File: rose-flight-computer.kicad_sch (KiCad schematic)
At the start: 17 parts

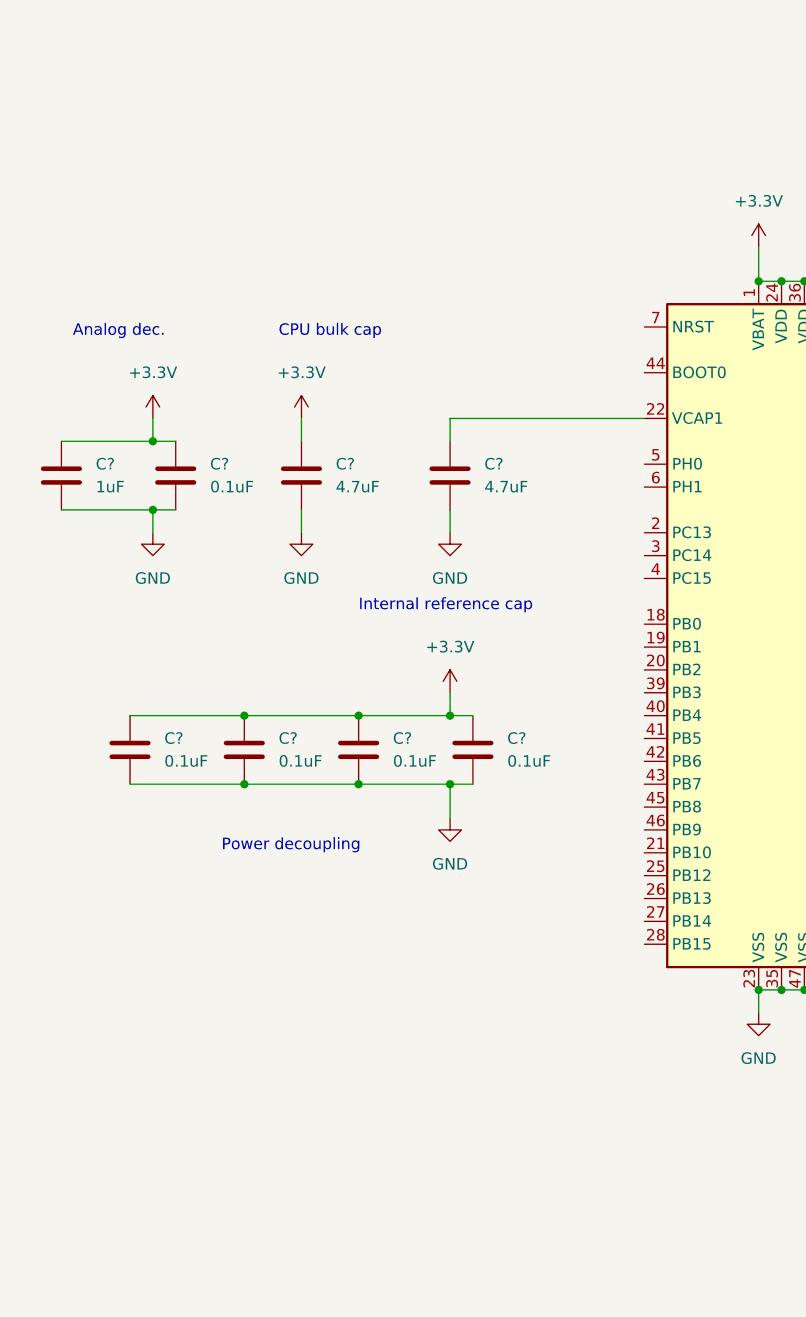
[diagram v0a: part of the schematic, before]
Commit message: Imported power circuit from old schematic
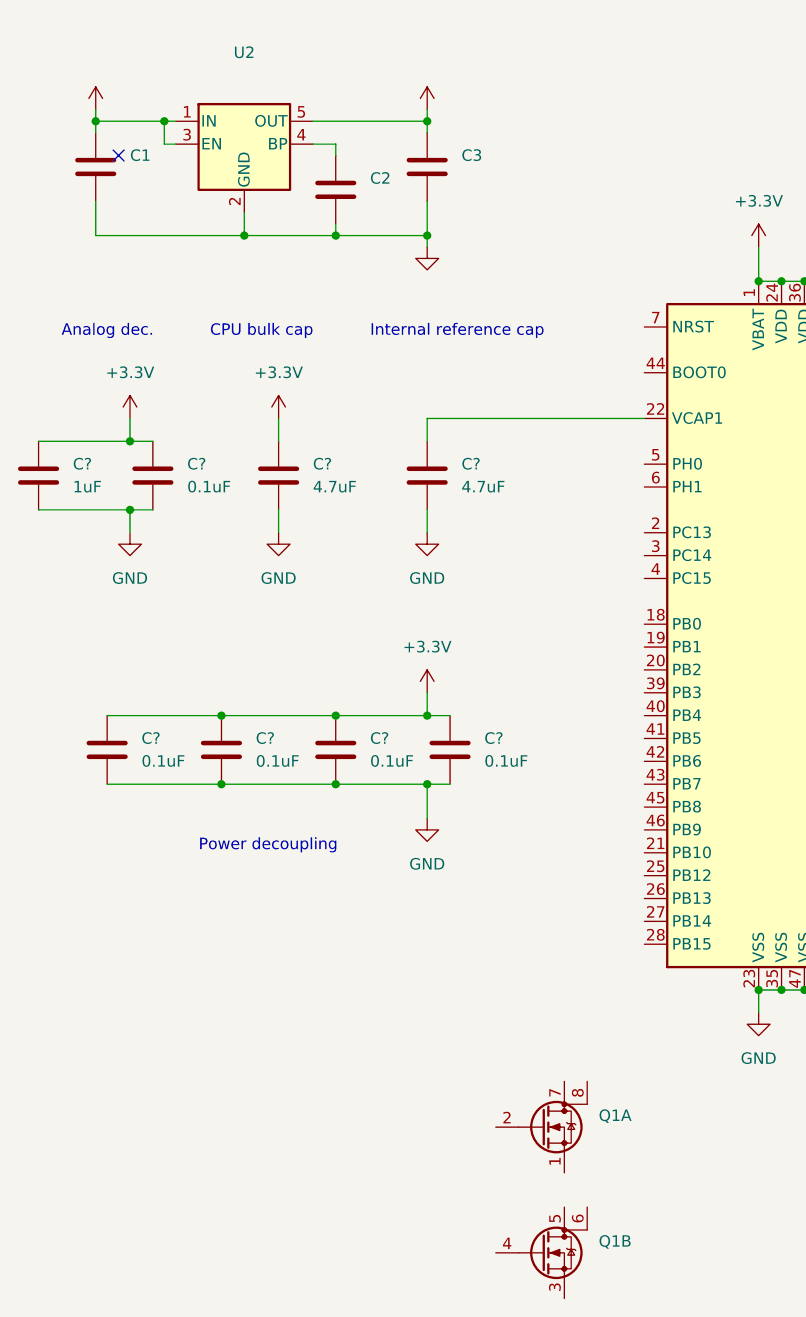
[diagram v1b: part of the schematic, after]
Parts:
- added C1, C2, C3: (no value), symbol Device:C
- added Q1: (no value), symbol Device:Q_Dual_NMOS_S1G1S2G2D2D2D1D1
- added U2: (no value), symbol Regulator_Linear:MIC5205-3.3YM5
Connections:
- net +3V3: now also C3.1, U2.5 (OUT)
- net GND: now also C1.2, C2.2, C3.2, U2.2 (GND)
- new net: C2.1, U2.4 (BP)
- new net +BATT: C1.1, U2.1 (IN), U2.3 (EN)
- no-connect marks 0 -> 1
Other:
- moved on the sheet: C?
